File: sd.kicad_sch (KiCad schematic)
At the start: 47 parts, among them J3 Micro_SD_Card, J4 Conn_01x08, Q1 DMG1032UV, Q2 BSS84, Q3 DMG1032UV, U11 SN74LVC1G14DRL, U12 TS3DDR4000ZBAR, U13 74AUC1G86, U14 GL3224-OIYxx, U15 25LCxxx-MC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

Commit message: sd.kicad_sch: fix power select PMOSes
Back-to-back configuration should use transitors from the same package.

Signed-off-by: Dominik Sliwa <dominik@sliwa.io>
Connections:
- net EXT_V_{DD}: now also Q3.1 (S); no longer Q1.6 (D)
- net SD_{MUX}_V_{DD}: now also Q1.1 (S); no longer Q3.6 (D)
- net ~SD_MUX_SEL: now also Q1.2 (G); no longer Q3.2 (G)
- net at Q1.4 (S), R10.2: now also Q1.6 (D); no longer Q3.1 (S)
- net at Q3.4 (S), R9.2: now also Q3.6 (D); no longer Q1.1 (S)
- net at Q3.5 (G), R25.2, R9.1: now also Q3.2 (G); no longer Q1.2 (G)
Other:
- moved on the sheet: Q1A, Q3A
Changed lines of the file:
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@@
     )
   )
-  (symbol (lib_id "Device:Q_Dual_PMOS_S1G1D2S2G2D1") (at 71.12 159.385 90) (unit 1)
+  (symbol (lib_id "Device:Q_Dual_PMOS_S1G1D2S2G2D1") (at 71.12 159.385 270) (mirror x) (unit 1)
     (in_bom yes) (on_board yes)
-    (property "Reference" "Q1" (id 0) (at 71.12 149.86 90))
-    (property "Value" "DMG1032UV" (id 1) (at 71.12 152.4 90))
+    (property "Reference" "Q3" (id 0) (at 71.755 149.86 90))
+    (property "Value" "DMG1032UV" (id 1) (at 71.755 152.4 90))
     (property "Footprint" "" (id 2) (at 71.12 158.115 0)
       (effects (font (size 1.27 1.27)) hide)
@@
     )
   )
-  (symbol (lib_id "Device:Q_Dual_PMOS_S1G1D2S2G2D1") (at 93.98 139.7 270) (mirror x) (unit 1)
+  (symbol (lib_id "Device:Q_Dual_PMOS_S1G1D2S2G2D1") (at 93.98 139.7 90) (unit 1)
     (in_bom yes) (on_board yes)
-    (property "Reference" "Q3" (id 0) (at 94.615 130.175 90))
-    (property "Value" "DMG1032UV" (id 1) (at 94.615 132.715 90))
+    (property "Reference" "Q1" (id 0) (at 93.98 130.175 90))
+    (property "Value" "DMG1032UV" (id 1) (at 93.98 132.715 90))
     (property "Footprint" "" (id 2) (at 93.98 138.43 0)
       (effects (font (size 1.27 1.27)) hide)

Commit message: SDReWire: Footprint assigment
Signed-off-by: Dominik Sliwa <dominik@sliwa.io>
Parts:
- C44: footprint Capacitor_SMD:C_0603_1608Metric -> Capacitor_SMD:C_0402_1005Metric
- C54: footprint Capacitor_SMD:C_0201_0603Metric -> Capacitor_SMD:C_0402_1005Metric
- Q1, Q3: footprint (none) -> Package_TO_SOT_SMD:SOT-563
- RN1: footprint (none) -> Resistor_SMD:R_0402_1005Metric
- Y2: footprint (none) -> Oscillator:Oscillator_SMD_Abracon_ASCO-4Pin_1.6x1.2mm
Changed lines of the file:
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@@
       (effects (font (size 1.27 1.27)) (justify left))
     )
-    (property "Footprint" "Capacitor_SMD:C_0603_1608Metric" (id 2) (at 104.775 182.245 0)
+    (property "Footprint" "Capacitor_SMD:C_0402_1005Metric" (id 2) (at 104.775 182.245 0)
       (effects (font (size 1.27 1.27)) hide)
     )
@@
       (effects (font (size 1.27 1.27)) (justify left))
     )
-    (property "Footprint" "Capacitor_SMD:C_0201_0603Metric" (id 2) (at 238.76 28.575 0)
+    (property "Footprint" "Capacitor_SMD:C_0402_1005Metric" (id 2) (at 238.76 28.575 0)
       (effects (font (size 1.27 1.27)) hide)
     )
@@
     (property "Reference" "RN1" (id 0) (at 40.005 182.245 90))
     (property "Value" "10k" (id 1) (at 40.005 186.055 90))
-    (property "Footprint" "" (id 2) (at 40.005 186.182 90)
+    (property "Footprint" "Resistor_SMD:R_0402_1005Metric" (id 2) (at 40.005 186.182 90)
       (effects (font (size 1.27 1.27)) hide)
     )
@@
     (property "Reference" "RN1" (id 0) (at 52.705 189.865 90))
     (property "Value" "10k" (id 1) (at 52.705 193.675 90))
-    (property "Footprint" "" (id 2) (at 52.705 189.738 90)
+    (property "Footprint" "Resistor_SMD:R_0402_1005Metric" (id 2) (at 52.705 189.738 90)
       (effects (font (size 1.27 1.27)) hide)
     )
@@
     (property "Reference" "RN1" (id 0) (at 252.095 75.565 90))
     (property "Value" "10k" (id 1) (at 252.095 80.01 90))
-    (property "Footprint" "" (id 2) (at 252.095 79.502 90)
+    (property "Footprint" "Resistor_SMD:R_0402_1005Metric" (id 2) (at 252.095 79.502 90)
       (effects (font (size 1.27 1.27)) hide)
     )
@@
       (effects (font (size 1.27 1.27)) (justify right))
     )
-    (property "Footprint" "" (id 2) (at 176.53 83.82 0)
+    (property "Footprint" "Oscillator:Oscillator_SMD_Abracon_ASCO-4Pin_1.6x1.2mm" (id 2) (at 176.53 83.82 0)
       (effects (font (size 1.27 1.27)) hide)
     )
@@
     (property "Reference" "Q3" (id 0) (at 71.755 149.86 90))
     (property "Value" "DMG1032UV" (id 1) (at 71.755 152.4 90))
-    (property "Footprint" "" (id 2) (at 71.12 158.115 0)
+    (property "Footprint" "Package_TO_SOT_SMD:SOT-563" (id 2) (at 71.12 158.115 0)
       (effects (font (size 1.27 1.27)) hide)
     )
@@
     (property "Reference" "Q1" (id 0) (at 80.645 130.175 90))
     (property "Value" "DMG1032UV" (id 1) (at 80.645 132.715 90))
-    (property "Footprint" "" (id 2) (at 80.01 138.43 0)
+    (property "Footprint" "Package_TO_SOT_SMD:SOT-563" (id 2) (at 80.01 138.43 0)
       (effects (font (size 1.27 1.27)) hide)
     )
@@
     (property "Reference" "Q3" (id 0) (at 84.455 149.86 90))
     (property "Value" "DMG1032UV" (id 1) (at 84.455 152.4 90))
-    (property "Footprint" "" (id 2) (at 83.82 158.115 0)
+    (property "Footprint" "Package_TO_SOT_SMD:SOT-563" (id 2) (at 83.82 158.115 0)
       (effects (font (size 1.27 1.27)) hide)
     )
@@
     (property "Reference" "Q1" (id 0) (at 93.98 130.175 90))
     (property "Value" "DMG1032UV" (id 1) (at 93.98 132.715 90))
-    (property "Footprint" "" (id 2) (at 93.98 138.43 0)
-      (effects (font (size 1.27 1.27)) hide)
-    )
+    (property "Footprint" "Package_TO_SOT_SMD:SOT-563" (id 2) (at 93.98 138.43 0)
+      (effects (font (size 1.27 1.27)) hide)
+    )

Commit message: SDReWire: rename FTDI_GPIO to SD_MUX_SEL and fix assigment
Resistor array had a wrong footprint

Signed-off-by: Dominik Sliwa <dominik@sliwa.io>
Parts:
- RN1: footprint Resistor_SMD:R_0402_1005Metric -> Resistor_SMD:R_Array_Convex_4x0402
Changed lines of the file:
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@@
     (property "Reference" "RN1" (id 0) (at 40.005 182.245 90))
     (property "Value" "10k" (id 1) (at 40.005 186.055 90))
-    (property "Footprint" "Resistor_SMD:R_0402_1005Metric" (id 2) (at 40.005 186.182 90)
+    (property "Footprint" "Resistor_SMD:R_Array_Convex_4x0402" (id 2) (at 40.005 186.182 90)
       (effects (font (size 1.27 1.27)) hide)
     )
@@
     (property "Reference" "RN1" (id 0) (at 52.705 189.865 90))
     (property "Value" "10k" (id 1) (at 52.705 193.675 90))
-    (property "Footprint" "Resistor_SMD:R_0402_1005Metric" (id 2) (at 52.705 189.738 90)
+    (property "Footprint" "Resistor_SMD:R_Array_Convex_4x0402" (id 2) (at 52.705 189.738 90)
       (effects (font (size 1.27 1.27)) hide)
     )
@@
     (property "Reference" "RN1" (id 0) (at 252.095 75.565 90))
     (property "Value" "10k" (id 1) (at 252.095 80.01 90))
-    (property "Footprint" "Resistor_SMD:R_0402_1005Metric" (id 2) (at 252.095 79.502 90)
+    (property "Footprint" "Resistor_SMD:R_Array_Convex_4x0402" (id 2) (at 252.095 79.502 90)
       (effects (font (size 1.27 1.27)) hide)
     )

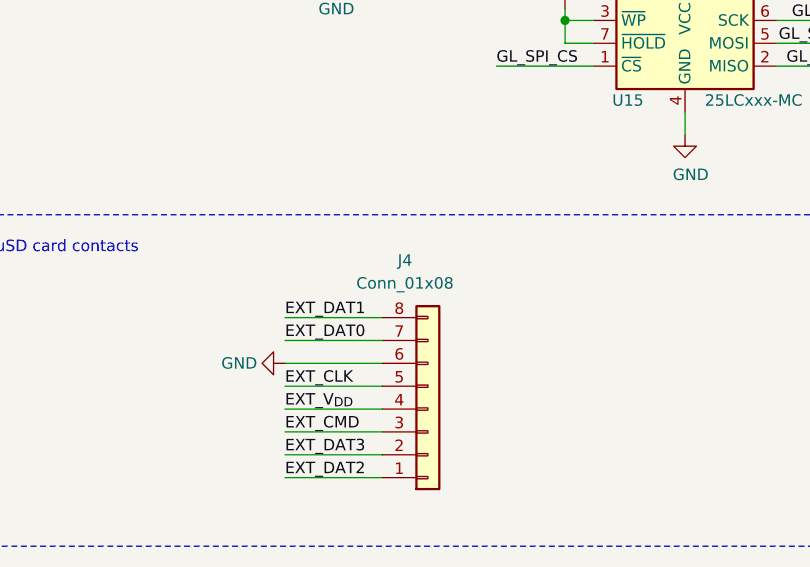
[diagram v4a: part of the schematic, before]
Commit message: SDReWire: add configurable link for gpio dir
Signed-off-by: Dominik Sliwa <dominik@sliwa.io>
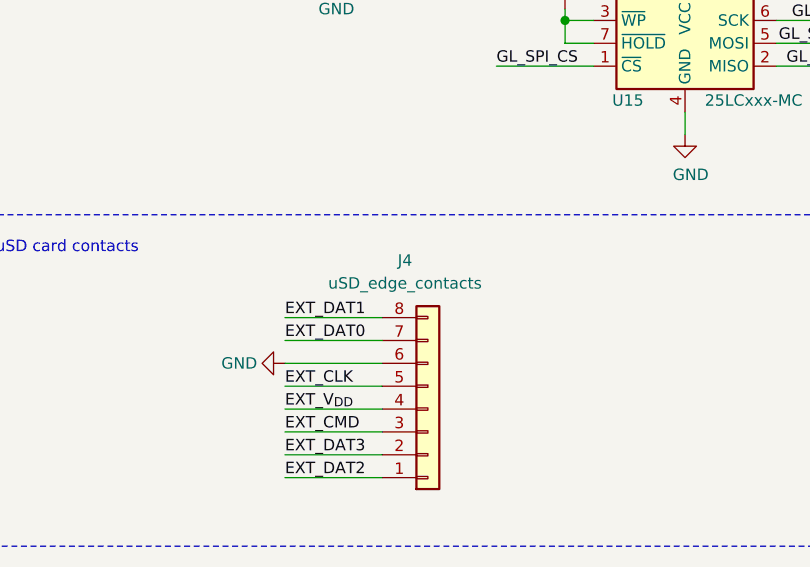
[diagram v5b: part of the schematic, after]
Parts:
- J4: value Conn_01x08 -> uSD_edge_contacts
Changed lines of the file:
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@@
   (junction (at 247.015 42.545) (diameter 1.016) (color 0 0 0 0))
   (junction (at 257.81 95.25) (diameter 1.016) (color 0 0 0 0))
+  (no_connect (at 95.25 62.23))
+  (no_connect (at 125.73 57.15))
+  (no_connect (at 125.73 100.33))
+  (no_connect (at 125.73 72.39))
+  (no_connect (at 125.73 52.07))
+  (no_connect (at 95.25 46.99))
+  (no_connect (at 95.25 57.15))
+  (no_connect (at 125.73 95.25))
+  (no_connect (at 125.73 85.09))
+  (no_connect (at 95.25 67.31))
+  (no_connect (at 125.73 90.17))
+  (no_connect (at 125.73 67.31))
   (no_connect (at 95.25 72.39))
-  (no_connect (at 125.73 67.31))
+  (no_connect (at 95.25 52.07))
+  (no_connect (at 125.73 105.41))
+  (no_connect (at 125.73 80.01))
+  (no_connect (at 125.73 46.99))
   (no_connect (at 125.73 62.23))
-  (no_connect (at 125.73 95.25))
-  (no_connect (at 125.73 46.99))
-  (no_connect (at 125.73 105.41))
-  (no_connect (at 125.73 57.15))
-  (no_connect (at 95.25 52.07))
-  (no_connect (at 125.73 80.01))
-  (no_connect (at 125.73 90.17))
-  (no_connect (at 95.25 62.23))
-  (no_connect (at 95.25 67.31))
-  (no_connect (at 95.25 46.99))
-  (no_connect (at 125.73 85.09))
-  (no_connect (at 125.73 72.39))
-  (no_connect (at 95.25 57.15))
-  (no_connect (at 125.73 100.33))
-  (no_connect (at 125.73 52.07))
   (wire (pts (xy 20.955 187.96) (xy 33.655 187.96))
     (stroke (width 0) (type solid) (color 0 0 0 0))
@@
     (in_bom yes) (on_board yes)
     (property "Reference" "J4" (id 0) (at 226.695 129.54 0))
-    (property "Value" "Conn_01x08" (id 1) (at 226.695 132.08 0))
+    (property "Value" "uSD_edge_contacts" (id 1) (at 226.695 132.08 0))
     (property "Footprint" "Custom:uSD_PCB" (id 2) (at 229.235 146.05 0)
       (effects (font (size 1.27 1.27)) hide)

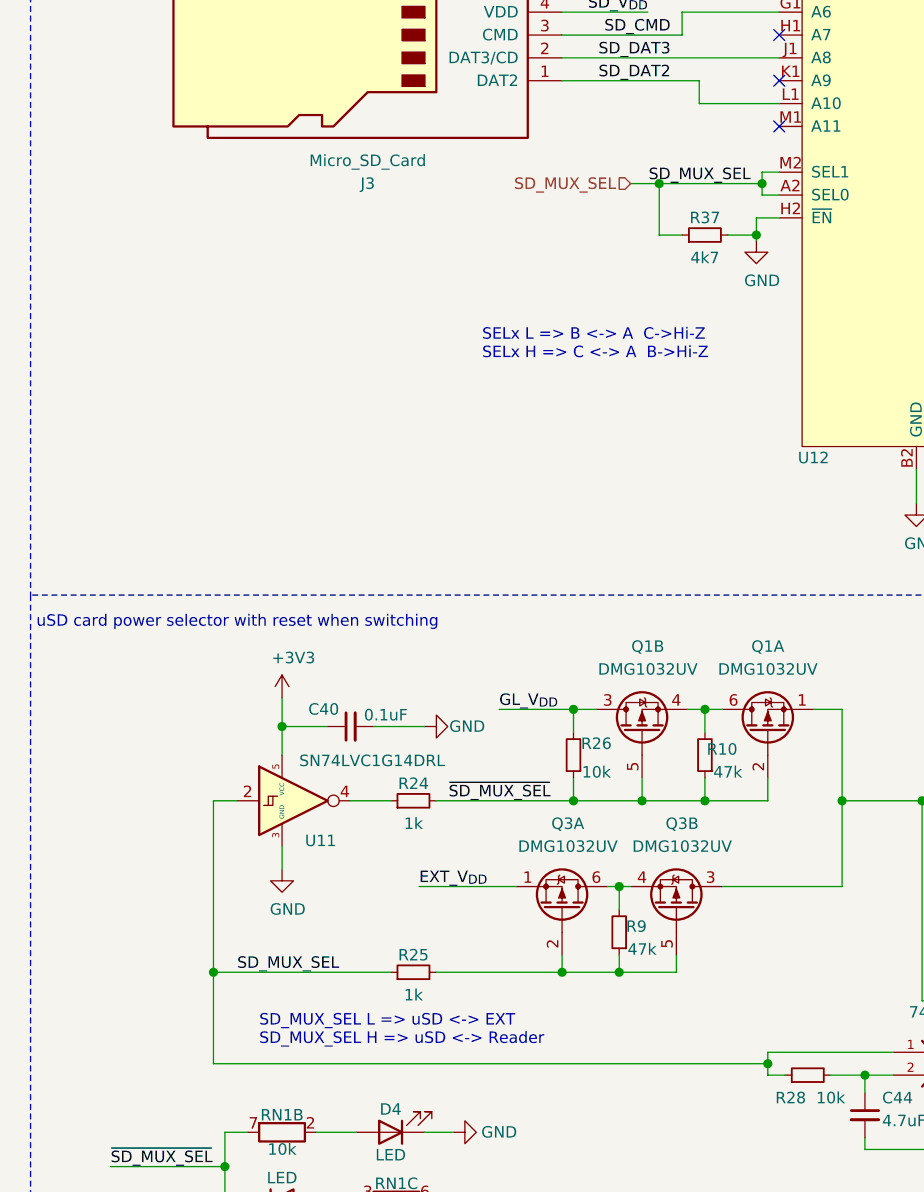
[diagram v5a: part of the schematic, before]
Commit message: sd.kicad_sch: improve SD_MUX_SEL net readability
Signed-off-by: Dominik Sliwa <dominik@sliwa.io>
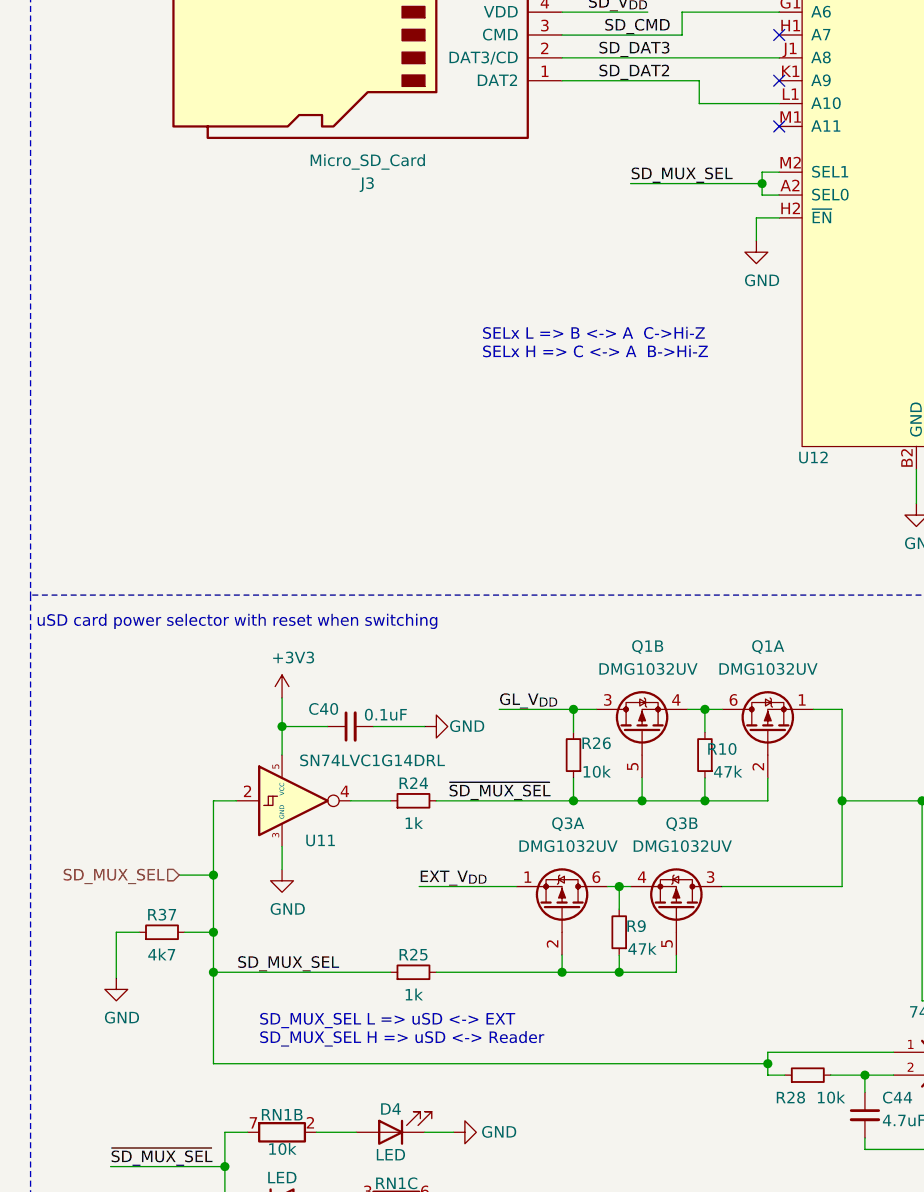
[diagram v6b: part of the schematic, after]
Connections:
- net GND: now also R37.1; no longer R37.2
- net SD_MUX_SEL: now also R37.2; no longer R37.1
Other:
- moved on the sheet: R37
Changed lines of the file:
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@@
   (page 1 5)
   (paper "A4")
+  (junction (at 32.385 155.575) (diameter 1.016) (color 0 0 0 0))
+  (junction (at 32.385 161.925) (diameter 1.016) (color 0 0 0 0))
   (junction (at 32.385 166.37) (diameter 1.016) (color 0 0 0 0))
   (junction (at 33.655 187.96) (diameter 1.016) (color 0 0 0 0))
@@
   (junction (at 81.915 22.225) (diameter 1.016) (color 0 0 0 0))
   (junction (at 81.915 31.75) (diameter 1.016) (color 0 0 0 0))
-  (junction (at 81.915 78.74) (diameter 1.016) (color 0 0 0 0))
   (junction (at 86.995 137.16) (diameter 1.016) (color 0 0 0 0))
   (junction (at 86.995 147.32) (diameter 1.016) (color 0 0 0 0))
   (junction (at 92.075 22.225) (diameter 1.016) (color 0 0 0 0))
   (junction (at 92.075 31.75) (diameter 1.016) (color 0 0 0 0))
-  (junction (at 92.71 84.455) (diameter 1.016) (color 0 0 0 0))
   (junction (at 93.345 78.74) (diameter 1.016) (color 0 0 0 0))
   (junction (at 93.98 176.53) (diameter 1.016) (color 0 0 0 0))
@@
     (stroke (width 0) (type solid) (color 0 0 0 0))
   )
+  (wire (pts (xy 21.59 161.925) (xy 21.59 167.005))
+    (stroke (width 0) (type solid) (color 0 0 0 0))
+  )
   (wire (pts (xy 22.86 44.45) (xy 22.86 47.625))
     (stroke (width 0) (type solid) (color 0 0 0 0))
   )
+  (wire (pts (xy 24.13 161.925) (xy 21.59 161.925))
+    (stroke (width 0) (type solid) (color 0 0 0 0))
+  )
   (wire (pts (xy 27.94 44.45) (xy 22.86 44.45))
     (stroke (width 0) (type solid) (color 0 0 0 0))
   )
-  (wire (pts (xy 32.385 147.32) (xy 32.385 166.37))
+  (wire (pts (xy 28.575 155.575) (xy 32.385 155.575))
+    (stroke (width 0) (type solid) (color 0 0 0 0))
+  )
+  (wire (pts (xy 29.21 161.925) (xy 32.385 161.925))
+    (stroke (width 0) (type solid) (color 0 0 0 0))
+  )
+  (wire (pts (xy 32.385 147.32) (xy 32.385 155.575))
+    (stroke (width 0) (type solid) (color 0 0 0 0))
+  )
+  (wire (pts (xy 32.385 155.575) (xy 32.385 161.925))
+    (stroke (width 0) (type solid) (color 0 0 0 0))
+  )
+  (wire (pts (xy 32.385 161.925) (xy 32.385 166.37))
     (stroke (width 0) (type solid) (color 0 0 0 0))
   )
@@
     (stroke (width 0) (type solid) (color 0 0 0 0))
   )
-  (wire (pts (xy 78.74 78.74) (xy 81.915 78.74))
+  (wire (pts (xy 78.74 78.74) (xy 93.345 78.74))
     (stroke (width 0) (type solid) (color 0 0 0 0))
   )
@@
     (stroke (width 0) (type solid) (color 0 0 0 0))
   )
-  (wire (pts (xy 81.915 78.74) (xy 93.345 78.74))
-    (stroke (width 0) (type solid) (color 0 0 0 0))
-  )
-  (wire (pts (xy 81.915 84.455) (xy 81.915 78.74))
-    (stroke (width 0) (type solid) (color 0 0 0 0))
-  )
   (wire (pts (xy 82.55 44.45) (xy 95.25 44.45))
     (stroke (width 0) (type solid) (color 0 0 0 0))
@@
     (stroke (width 0) (type solid) (color 0 0 0 0))
   )
-  (wire (pts (xy 84.455 84.455) (xy 81.915 84.455))
-    (stroke (width 0) (type solid) (color 0 0 0 0))
-  )
   (wire (pts (xy 85.09 137.16) (xy 86.995 137.16))
     (stroke (width 0) (type solid) (color 0 0 0 0))
@@
     (stroke (width 0) (type solid) (color 0 0 0 0))
   )
-  (wire (pts (xy 89.535 84.455) (xy 92.71 84.455))
-    (stroke (width 0) (type solid) (color 0 0 0 0))
-  )
   (wire (pts (xy 92.075 22.225) (xy 81.915 22.225))
     (stroke (width 0) (type solid) (color 0 0 0 0))
@@
     (stroke (width 0) (type solid) (color 0 0 0 0))
   )
-  (wire (pts (xy 92.71 82.55) (xy 92.71 84.455))
-    (stroke (width 0) (type solid) (color 0 0 0 0))
-  )
-  (wire (pts (xy 92.71 84.455) (xy 92.71 85.09))
+  (wire (pts (xy 92.71 82.55) (xy 92.71 85.09))
     (stroke (width 0) (type solid) (color 0 0 0 0))
   )
@@
     (effects (font (size 1.27 1.27)) (justify left bottom))
   )
+  (label "SD_MUX_SEL" (at 78.74 78.74 0)
+    (effects (font (size 1.27 1.27)) (justify left bottom))
+  )
   (label "SD_DAT1" (at 80.645 49.53 180)
     (effects (font (size 1.27 1.27)) (justify right bottom))
@@
     (effects (font (size 1.27 1.27)) (justify right bottom))
   )
-  (label "SD_MUX_SEL" (at 92.075 78.74 180)
-    (effects (font (size 1.27 1.27)) (justify right bottom))
-  )
   (label "SD_{MUX}_V_{DD}" (at 100.33 36.83 0)
     (effects (font (size 1.27 1.27)) (justify left bottom))
@@
     (effects (font (size 1.27 1.27)) (justify right bottom))
   )
-  (hierarchical_label "SD_MUX_SEL" (shape input) (at 78.74 78.74 180)
+  (hierarchical_label "SD_MUX_SEL" (shape input) (at 28.575 155.575 180)
     (effects (font (size 1.27 1.27)) (justify right))
   )
@@
     )
   )
+  (symbol (lib_id "power:GND") (at 21.59 167.005 0) (unit 1)
+    (in_bom yes) (on_board yes)
+    (property "Reference" "#PWR?" (id 0) (at 21.59 173.355 0)
+      (effects (font (size 1.27 1.27)) hide)
+    )
+    (property "Value" "GND" (id 1) (at 22.225 171.45 0))
+    (property "Footprint" "" (id 2) (at 21.59 167.005 0)
+      (effects (font (size 1.27 1.27)) hide)
+    )
+    (property "Datasheet" "" (id 3) (at 21.59 167.005 0)
+      (effects (font (size 1.27 1.27)) hide)
+    )
+  )
   (symbol (lib_id "power:GND") (at 22.86 47.625 0) (unit 1)
     (in_bom yes) (on_board yes)
@@
     )
     (property "Datasheet" "" (id 3) (at 271.78 77.47 0)
+      (effects (font (size 1.27 1.27)) hide)
+    )
+  )
+  (symbol (lib_id "Device:R_Small") (at 26.67 161.925 90) (unit 1)
+    (in_bom yes) (on_board yes)
+    (property "Reference" "R37" (id 0) (at 26.67 160.02 90))
+    (property "Value" "4k7" (id 1) (at 26.67 164.465 90))
+    (property "Footprint" "Resistor_SMD:R_0402_1005Metric" (id 2) (at 26.67 161.925 0)
+      (effects (font (size 1.27 1.27)) hide)
+    )
+    (property "Datasheet" "~" (id 3) (at 26.67 161.925 0)
       (effects (font (size 1.27 1.27)) hide)
     )
@@
       (effects (font (size 1.27 1.27)) hide)
     )
-  )
-  (symbol (lib_id "Device:R_Small") (at 86.995 84.455 90) (unit 1)
-    (in_bom yes) (on_board yes)
-    (property "Reference" "R37" (id 0) (at 86.995 82.55 90))
-    (property "Value" "4k7" (id 1) (at 86.995 86.995 90))
-    (property "Footprint" "Resistor_SMD:R_0402_1005Metric" (id 2) (at 86.995 84.455 0)
-      (effects (font (size 1.27 1.27)) hide)
-    )
-    (property "Datasheet" "~" (id 3) (at 86.995 84.455 0)
-      (effects (font (size 1.27 1.27)) hide)
-    )
